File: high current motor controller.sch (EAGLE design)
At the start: 51 parts, among them IC1 LM2676S, Q1 IPT004N03L, Q2 IPT004N03L, Q3 IPT004N03L, Q4 IPT004N03L

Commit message: Added library for power and motor connectors; updated schematic with connectors
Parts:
- removed MOTOR+, MOTOR-: (no value), pinhead:PINHD-1X1
- added U$3: MOLEX_2PIN_50A, connector:MOLEX_2PIN_50A
- added U$4: TE_2PIN_125A, connector:TE_2PIN_125A
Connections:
- net AHS: now also U$3.P$1; no longer MOTOR+.1
- net BHS: now also U$3.P$2; no longer MOTOR-.1
- net GND: now also U$4.P$2
- net VIN: now also U$4.P$1
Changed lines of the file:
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@@
 <part name="D14" library="diode" deviceset="SCHOTTKY-DIODE" device="SMC"/>
 <part name="D15" library="diode" deviceset="SCHOTTKY-DIODE" device="SMC"/>
-<part name="MOTOR+" library="pinhead" deviceset="PINHD-1X1" device=""/>
-<part name="MOTOR-" library="pinhead" deviceset="PINHD-1X1" device=""/>
 <part name="D9" library="semicon-smd-ipc" deviceset="D-" device="SOD123"/>
 <part name="Q1" library="IPT004N03L" deviceset="IPT004N03L" device=""/>
@@
 <part name="C9" library="resistor" deviceset="C-US" device="C0805" value="4.7u"/>
 <part name="C10" library="resistor" deviceset="C-US" device="C0805" value="4.7u"/>
+<part name="U$3" library="connector" deviceset="MOLEX_2PIN_50A" device=""/>
+<part name="U$4" library="connector" deviceset="TE_2PIN_125A" device=""/>
 </parts>
 <sheets>
@@
 <instance part="D14" gate="G$1" x="68.58" y="27.94" rot="R270"/>
 <instance part="D15" gate="G$1" x="91.44" y="82.55" rot="R90"/>
-<instance part="MOTOR+" gate="G$1" x="59.69" y="43.18"/>
-<instance part="MOTOR-" gate="G$1" x="64.77" y="43.18" rot="R180"/>
 <instance part="D9" gate="G$1" x="10.16" y="45.72" rot="R270"/>
 <instance part="Q1" gate="G$1" x="27.94" y="66.04"/>
@@
 <instance part="C9" gate="G$1" x="-114.3" y="-86.36"/>
 <instance part="C10" gate="G$1" x="-124.46" y="-86.36"/>
+<instance part="U$3" gate="G$1" x="-96.52" y="43.18"/>
+<instance part="U$4" gate="G$1" x="-96.52" y="-5.08"/>
 </instances>
 <busses>
@@
 <pinref part="C2" gate="G$1" pin="1"/>
 <junction x="50.8" y="35.56"/>
-<wire x1="50.8" y1="35.56" x2="50.8" y2="43.18" width="0.1524" layer="91"/>
-<wire x1="50.8" y1="43.18" x2="50.8" y2="50.8" width="0.1524" layer="91"/>
-<wire x1="50.8" y1="43.18" x2="57.15" y2="43.18" width="0.1524" layer="91"/>
-<junction x="50.8" y="43.18"/>
-<pinref part="MOTOR+" gate="G$1" pin="1"/>
+<wire x1="50.8" y1="35.56" x2="50.8" y2="50.8" width="0.1524" layer="91"/>
 <label x="29.21" y="52.07" size="1.27" layer="95" rot="R180" xref="yes"/>
 <wire x1="29.21" y1="52.07" x2="33.02" y2="52.07" width="0.1524" layer="91"/>
@@
 <label x="63.5" y="-12.7" size="1.778" layer="95" xref="yes"/>
 </segment>
+<segment>
+<pinref part="U$3" gate="G$1" pin="P$1"/>
+<wire x1="-106.68" y1="43.18" x2="-106.68" y2="27.94" width="0.1524" layer="91"/>
+<label x="-106.68" y="27.94" size="1.778" layer="95" rot="R270" xref="yes"/>
+</segment>
 </net>
 <net name="N$6" class="0">
@@
 <wire x1="73.66" y1="35.56" x2="73.66" y2="30.48" width="0.1524" layer="91"/>
 <pinref part="C1" gate="G$1" pin="2"/>
-<wire x1="73.66" y1="50.8" x2="73.66" y2="43.18" width="0.1524" layer="91"/>
 <junction x="73.66" y="35.56"/>
-<wire x1="73.66" y1="43.18" x2="73.66" y2="35.56" width="0.1524" layer="91"/>
+<wire x1="73.66" y1="50.8" x2="73.66" y2="35.56" width="0.1524" layer="91"/>
 <wire x1="91.44" y1="50.8" x2="91.44" y2="52.07" width="0.1524" layer="91"/>
 <pinref part="D7" gate="G$1" pin="C"/>
@@
 <wire x1="68.58" y1="30.48" x2="73.66" y2="30.48" width="0.1524" layer="91"/>
 <pinref part="D14" gate="G$1" pin="A"/>
-<wire x1="67.31" y1="43.18" x2="73.66" y2="43.18" width="0.1524" layer="91"/>
-<junction x="73.66" y="43.18"/>
-<pinref part="MOTOR-" gate="G$1" pin="1"/>
 <wire x1="91.44" y1="52.07" x2="97.79" y2="52.07" width="0.1524" layer="91"/>
 <junction x="91.44" y="52.07"/>
@@
 <junction x="139.7" y="-15.24"/>
 <label x="143.51" y="-15.24" size="1.778" layer="95" xref="yes"/>
+</segment>
+<segment>
+<pinref part="U$3" gate="G$1" pin="P$2"/>
+<wire x1="-86.36" y1="43.18" x2="-86.36" y2="27.94" width="0.1524" layer="91"/>
+<label x="-86.36" y="27.94" size="1.778" layer="95" rot="R270" xref="yes"/>
 </segment>
 </net>
@@
 <junction x="-114.3" y="-91.44"/>
 </segment>
+<segment>
+<wire x1="-86.36" y1="0" x2="-86.36" y2="-5.08" width="0.1524" layer="91"/>
+<label x="-86.36" y="-20.32" size="1.778" layer="95" rot="R270" xref="yes"/>
+<pinref part="U$4" gate="G$1" pin="P$2"/>
+<wire x1="-86.36" y1="-5.08" x2="-86.36" y2="-20.32" width="0.1524" layer="91"/>
+<junction x="-86.36" y="-5.08"/>
+</segment>
 </net>
 <net name="12V" class="0">
@@
 <junction x="-114.3" y="-81.28"/>
 </segment>
-</net>
+<segment>
+<wire x1="-106.68" y1="0" x2="-106.68" y2="-5.08" width="0.1524" layer="91"/>
+<label x="-106.68" y="-20.32" size="1.778" layer="95" rot="R270" xref="yes"/>
+<pinref part="U$4" gate="G$1" pin="P$1"/>
+<wire x1="-106.68" y1="-5.08" x2="-106.68" y2="-20.32" width="0.1524" layer="91"/>
+<junction x="-106.68" y="-5.08"/>
+</segment>
+</net>

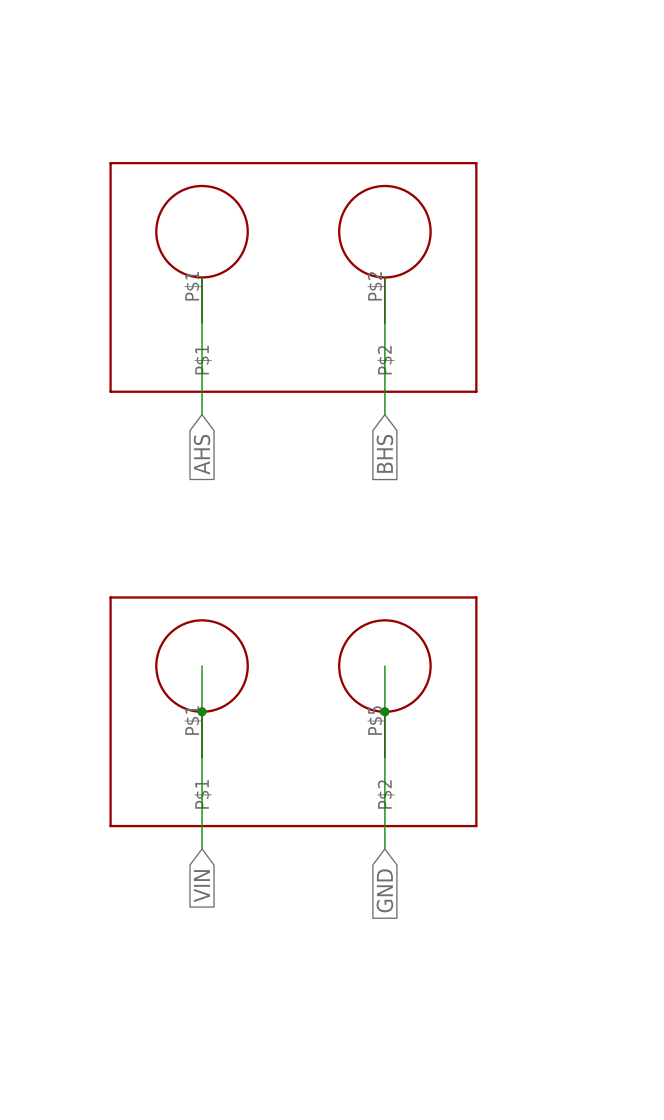
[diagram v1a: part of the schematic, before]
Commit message: Updated connector library to use all pads of power connector
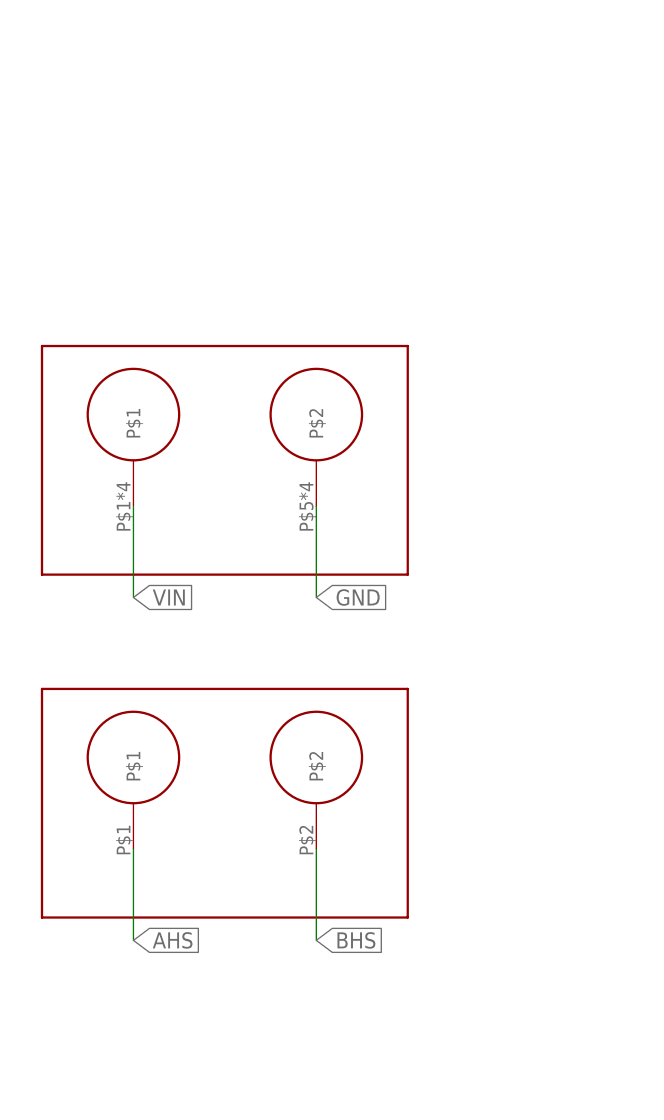
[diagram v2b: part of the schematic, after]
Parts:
- U$3: value MOLEX_2PIN_50A -> TE_2PIN_125A; device connector:MOLEX_2PIN_50A -> connector:TE_2PIN_125A
- U$4: value TE_2PIN_125A -> MOLEX_2PIN_50A; device connector:TE_2PIN_125A -> connector:MOLEX_2PIN_50A
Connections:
- net AHS: now also U$4.P$1; no longer U$3.P$1
- net BHS: now also U$4.P$2; no longer U$3.P$2
- net GND: now also U$3.P$2; no longer U$4.P$2
- net VIN: now also U$3.P$1; no longer U$4.P$1
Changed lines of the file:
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@@
 <part name="C9" library="resistor" deviceset="C-US" device="C0805" value="4.7u"/>
 <part name="C10" library="resistor" deviceset="C-US" device="C0805" value="4.7u"/>
-<part name="U$3" library="connector" deviceset="MOLEX_2PIN_50A" device=""/>
-<part name="U$4" library="connector" deviceset="TE_2PIN_125A" device=""/>
+<part name="U$3" library="connector" deviceset="TE_2PIN_125A" device=""/>
+<part name="U$4" library="connector" deviceset="MOLEX_2PIN_50A" device=""/>
 </parts>
 <sheets>
@@
 <instance part="C9" gate="G$1" x="-114.3" y="-86.36"/>
 <instance part="C10" gate="G$1" x="-124.46" y="-86.36"/>
-<instance part="U$3" gate="G$1" x="-96.52" y="43.18"/>
-<instance part="U$4" gate="G$1" x="-96.52" y="-5.08"/>
+<instance part="U$3" gate="G$1" x="-104.14" y="22.86"/>
+<instance part="U$4" gate="G$1" x="-104.14" y="-15.24"/>
 </instances>
 <busses>
@@
 </segment>
 <segment>
-<pinref part="U$3" gate="G$1" pin="P$1"/>
-<wire x1="-106.68" y1="43.18" x2="-106.68" y2="27.94" width="0.1524" layer="91"/>
-<label x="-106.68" y="27.94" size="1.778" layer="95" rot="R270" xref="yes"/>
+<pinref part="U$4" gate="G$1" pin="P$1"/>
+<wire x1="-114.3" y1="-20.32" x2="-114.3" y2="-30.48" width="0.1524" layer="91"/>
+<label x="-114.3" y="-30.48" size="1.778" layer="95" xref="yes"/>
 </segment>
 </net>
@@
 </segment>
 <segment>
-<pinref part="U$3" gate="G$1" pin="P$2"/>
-<wire x1="-86.36" y1="43.18" x2="-86.36" y2="27.94" width="0.1524" layer="91"/>
-<label x="-86.36" y="27.94" size="1.778" layer="95" rot="R270" xref="yes"/>
+<pinref part="U$4" gate="G$1" pin="P$2"/>
+<wire x1="-93.98" y1="-20.32" x2="-93.98" y2="-30.48" width="0.1524" layer="91"/>
+<label x="-93.98" y="-30.48" size="1.778" layer="95" xref="yes"/>
 </segment>
 </net>
@@
 </segment>
 <segment>
-<wire x1="-86.36" y1="0" x2="-86.36" y2="-5.08" width="0.1524" layer="91"/>
-<label x="-86.36" y="-20.32" size="1.778" layer="95" rot="R270" xref="yes"/>
-<pinref part="U$4" gate="G$1" pin="P$2"/>
-<wire x1="-86.36" y1="-5.08" x2="-86.36" y2="-20.32" width="0.1524" layer="91"/>
-<junction x="-86.36" y="-5.08"/>
+<pinref part="U$3" gate="G$1" pin="P$2"/>
+<wire x1="-93.98" y1="17.78" x2="-93.98" y2="7.62" width="0.1524" layer="91"/>
+<label x="-93.98" y="7.62" size="1.778" layer="95" xref="yes"/>
 </segment>
 </net>
@@
 </segment>
 <segment>
-<wire x1="-106.68" y1="0" x2="-106.68" y2="-5.08" width="0.1524" layer="91"/>
-<label x="-106.68" y="-20.32" size="1.778" layer="95" rot="R270" xref="yes"/>
-<pinref part="U$4" gate="G$1" pin="P$1"/>
-<wire x1="-106.68" y1="-5.08" x2="-106.68" y2="-20.32" width="0.1524" layer="91"/>
-<junction x="-106.68" y="-5.08"/>
-</segment>
-</net>
+<pinref part="U$3" gate="G$1" pin="P$1"/>
+<wire x1="-114.3" y1="17.78" x2="-114.3" y2="7.62" width="0.1524" layer="91"/>
+<label x="-114.3" y="7.62" size="1.778" layer="95" xref="yes"/>
+</segment>
+</net>
